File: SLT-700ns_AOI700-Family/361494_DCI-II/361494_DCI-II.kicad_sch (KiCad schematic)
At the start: 7 parts, among them T1 CB, T2 CB, U1 12-Pin_SLx_Can

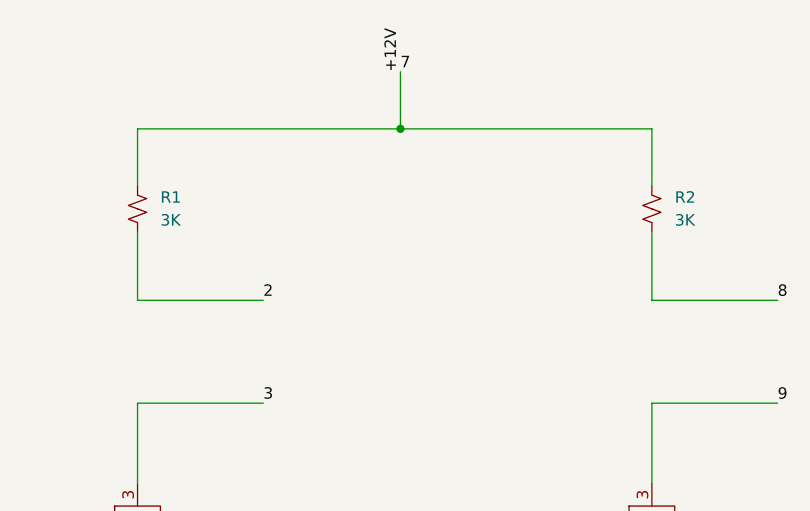
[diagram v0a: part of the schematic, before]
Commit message: Add can P/N to schematics for SLT-700
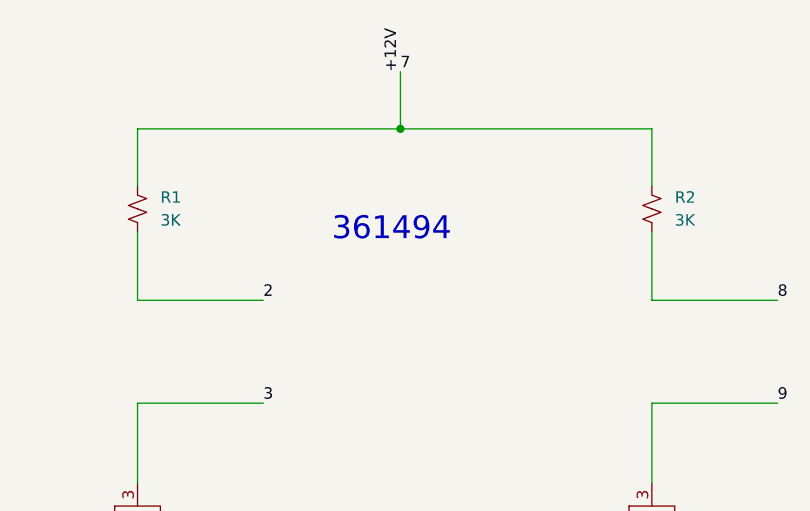
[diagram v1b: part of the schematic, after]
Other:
- note added: "361494"
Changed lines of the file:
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@@
     (stroke (width 0) (type default) (color 0 0 0 0))
+  )
+  (text "361494" (at 120.65 57.15 0)
+    (effects (font (size 2.54 2.54)) (justify left bottom))
   )
   (label "8" (at 170.18 63.5 0)
